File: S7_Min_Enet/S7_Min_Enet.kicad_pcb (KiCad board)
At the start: 4 copper layers, 62 x 42 mm, 47 parts, among them J1 USB_B_Micro, J2 Conn_02x15_Odd_Even, J3 J1B1211CCD, U1 FT230XS, U2 DP83848J, Y1 25MHz

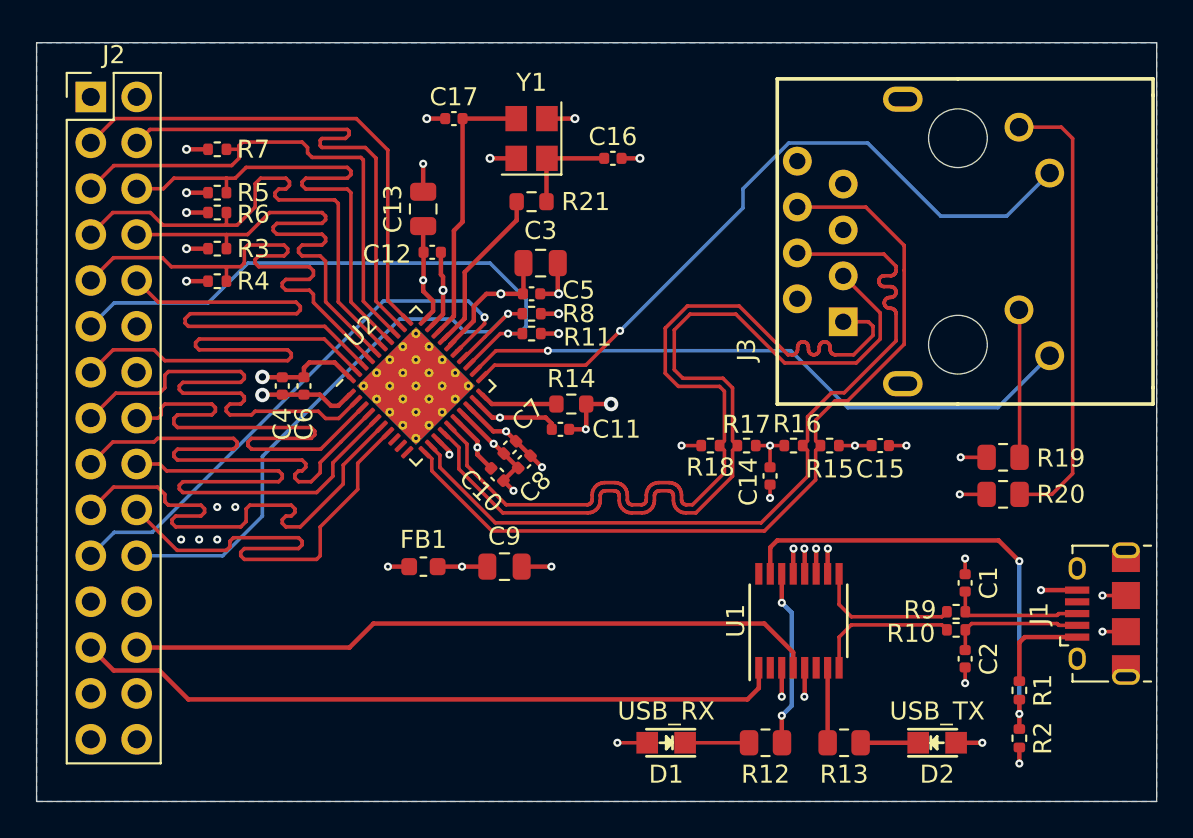
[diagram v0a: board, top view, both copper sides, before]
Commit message: Added gerbers for rev D main board and rev A ethernet board, schematic PDF for ethernet
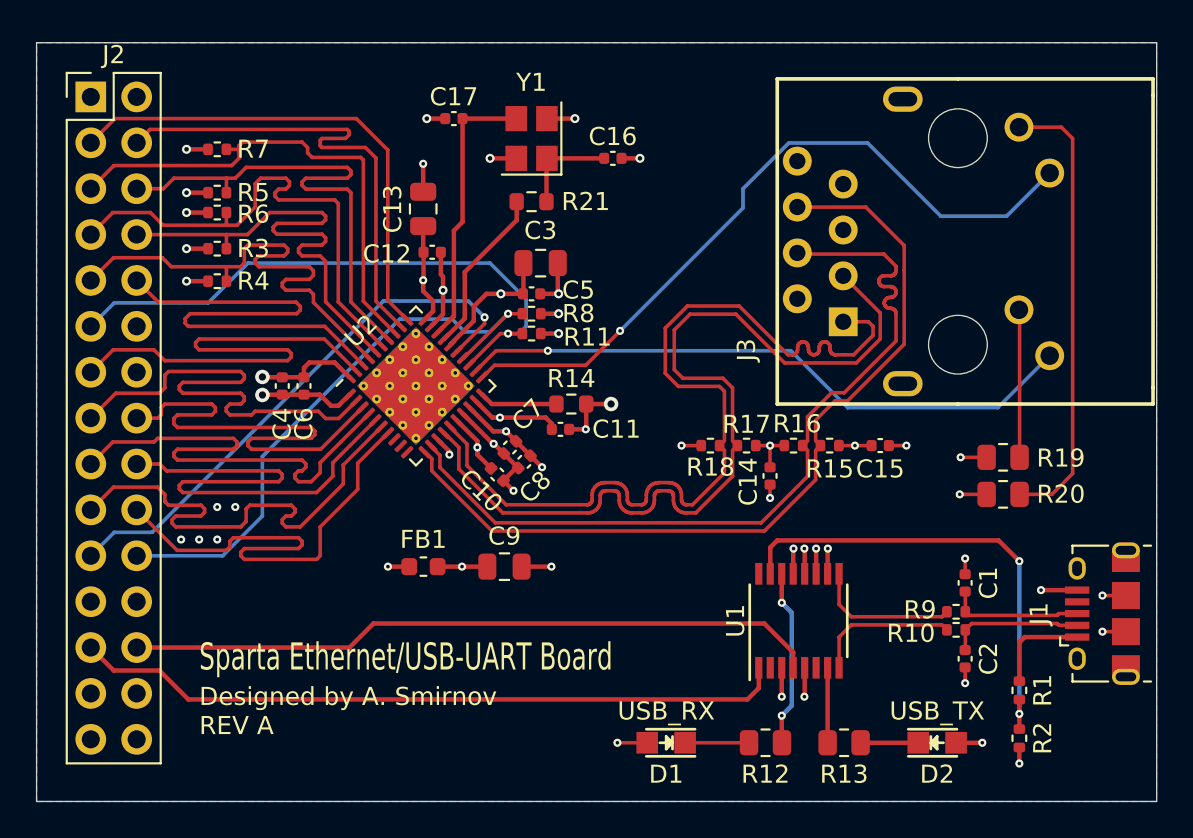
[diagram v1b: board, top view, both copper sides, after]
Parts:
- added REF**: KiCad-Logo2_8mm_SilkScreen, Symbol:KiCad-Logo2_8mm_SilkScreen, B.Cu at (130.2, 108.0)
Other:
- board text added: "Designed by A. Smirnov REV A"
- board text added: "Sparta Ethernet/USB-UART Board"

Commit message: revision B - fixed USB connection
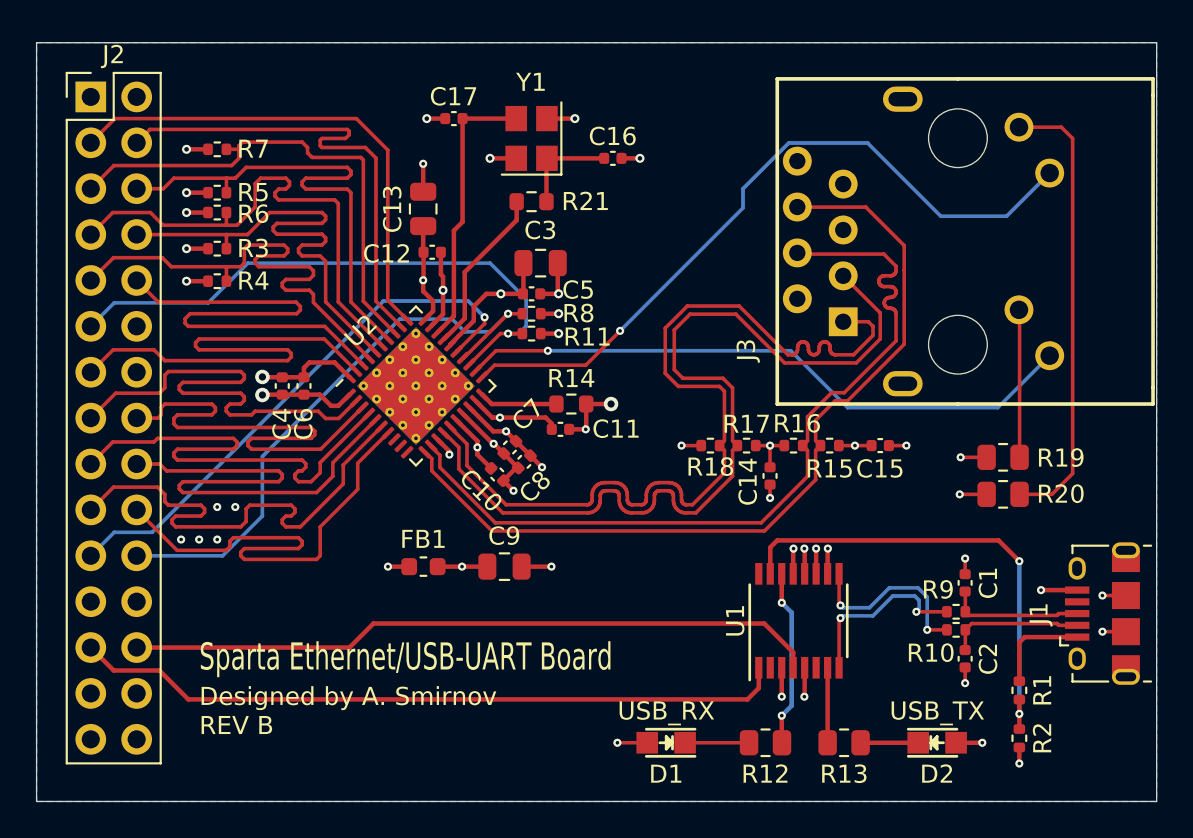
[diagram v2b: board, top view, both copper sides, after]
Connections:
- U1 pad 8: /USB- -> /USB+
- U1 pad 9: /USB+ -> /USB-
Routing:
- net /USB-: track 8.06 -> 10.2 mm, vias 0 -> 2
- net /USB+: track 8.06 -> 10.1 mm, vias 0 -> 2
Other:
- board text added: "Designed by A. Smirnov REV B"
- board text removed: "Designed by A. Smirnov REV A"

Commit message: made some resistors DNP, updated schematics and assembly docs
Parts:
- R3, R4, R5, R6: value 2.2K -> DNP
